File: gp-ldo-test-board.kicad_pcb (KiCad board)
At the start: 2 copper layers, 38.1 x 25.4 mm, 58 parts, among them J1 Conn_01x03, J2 Conn_01x02, J3 Conn_01x06, J4 Conn_01x02, J5 Conn_01x06, J6 Conn_01x02, J7 Conn_01x02, J8 Conn_01x02, J9 Conn_01x02, Q1 Q_PMOS_GSD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

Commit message: initial route draft
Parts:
- moved R3 9.96 mm to (51.6, 59.8), turned to 270 degrees
- moved R4 9.05 mm to (51.6, 63.3), turned to 270 degrees
- moved D3 5.50 mm to (79.9, 57.0)
- moved D5 5.50 mm to (79.9, 67.0)
- moved D7 5.50 mm to (79.9, 59.0)
- moved D9 5.50 mm to (79.9, 69.0)
- moved R10 5.50 mm to (77.0, 57.0)
- moved R12 5.50 mm to (77.0, 67.0)
- moved R14 5.50 mm to (77.0, 59.0)
- moved R16 5.50 mm to (77.0, 69.0)
- moved J6 5.08 mm to (86.3, 56.9)
- moved J7 5.08 mm to (86.3, 51.8)
- moved J8 5.08 mm to (86.3, 67.0)
- moved J9 5.08 mm to (86.3, 61.9)
- moved D10 4.50 mm to (79.9, 64.0)
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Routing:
- net /V_3.3_MGMT: track 0.00 -> 79.2 mm, vias 0 -> 1
- net +5V: track 0.00 -> 71.5 mm, vias 0 -> 2
- net GND: track 0.00 -> 45.1 mm, vias 0 -> 13
- net /SLG1_SCL: track 0.00 -> 32.8 mm, vias 0 -> 1
- net /CTRL_SDA: track 0.00 -> 27.0 mm, vias 0 -> 2
- net /V_Vccio1: track 0.00 -> 26.0 mm
- net /SLG1_SDA: track 0.00 -> 25.7 mm, vias 0 -> 1
- net /CTRL_SCL: track 0.00 -> 25.3 mm, vias 0 -> 2
- net /V_Vccio2: track 0.00 -> 24.8 mm
- net Net-(J5-Pad1): track 0.00 -> 24.7 mm, vias 0 -> 1
- net /V_3.3_MGMT_FAULT: track 0.00 -> 24.5 mm, vias 0 -> 2
- net /V_1.8_Vcore: track 0.00 -> 21.9 mm
- net Net-(J3-Pad5): track 0.00 -> 21.5 mm, vias 0 -> 1
- net Net-(Q1-Pad3): track 0.00 -> 17.1 mm, vias 0 -> 3
- net /V_Vccio1_FAULT: track 0.00 -> 14.4 mm, vias 0 -> 2
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- added copper zone on B.Cu, net GND
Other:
- net class power added: clearance 0.1524, trace_width 0.254, via_dia 0.762, via_drill 0.381

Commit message: route major cleanup
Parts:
- moved TP4 2.50 mm to (64.0, 51.6)
- moved D1 2.50 mm to (58.5, 72.9)
- moved D2 2.50 mm to (61.0, 72.9)
- moved R7 2.50 mm to (58.5, 70.0)
- moved R8 2.50 mm to (61.0, 70.0)
- moved TP3 0.30 mm to (64.0, 53.8)
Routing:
- net /AUX_LED_1: track 11.8 -> 5.86 mm
- net /AUX_LED_0: track 5.69 -> 9.05 mm
- net +5V: track 71.5 -> 68.5 mm
- net /V_1.8_Vcore_FAULT: track 11.3 -> 14.2 mm
- net /SLG1_SCL: track 32.8 -> 30.0 mm
- net Net-(Q1-Pad3): track 17.1 -> 14.5 mm
- net /CTRL_SDA: track 27.0 -> 25.4 mm, vias 2 -> 1
- net /CTRL_SCL: track 25.3 -> 23.9 mm, vias 2 -> 1
- net Net-(J3-Pad5): track 21.5 -> 22.5 mm
- net Net-(J3-Pad1): track 7.26 -> 8.26 mm, vias 1 -> 0
- net Net-(TP1-Pad1): track 4.57 -> 3.59 mm
- net GND: track 45.1 -> 44.3 mm
- net /SLG0_SDA: track 11.8 -> 12.5 mm
- net /V_Vccio1_FAULT: track 14.4 -> 13.7 mm

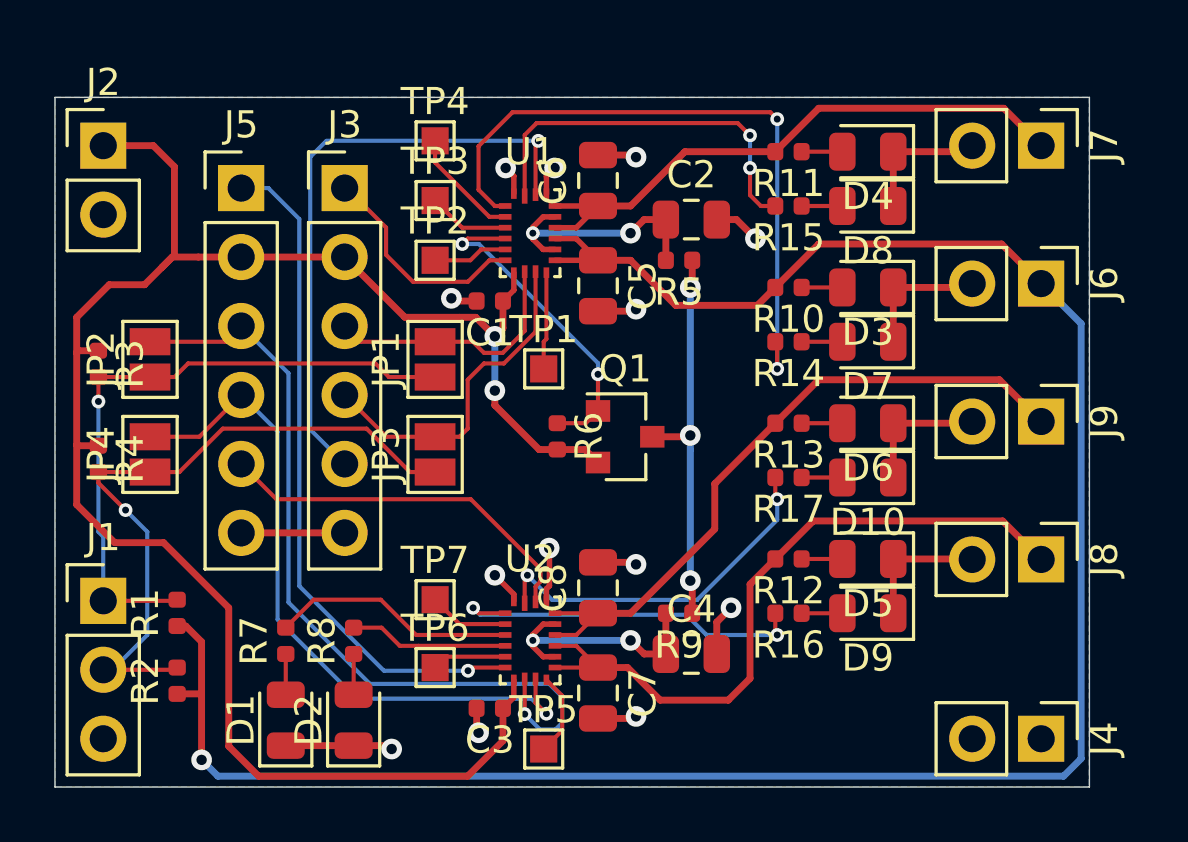
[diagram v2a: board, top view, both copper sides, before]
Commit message: silk cleanup
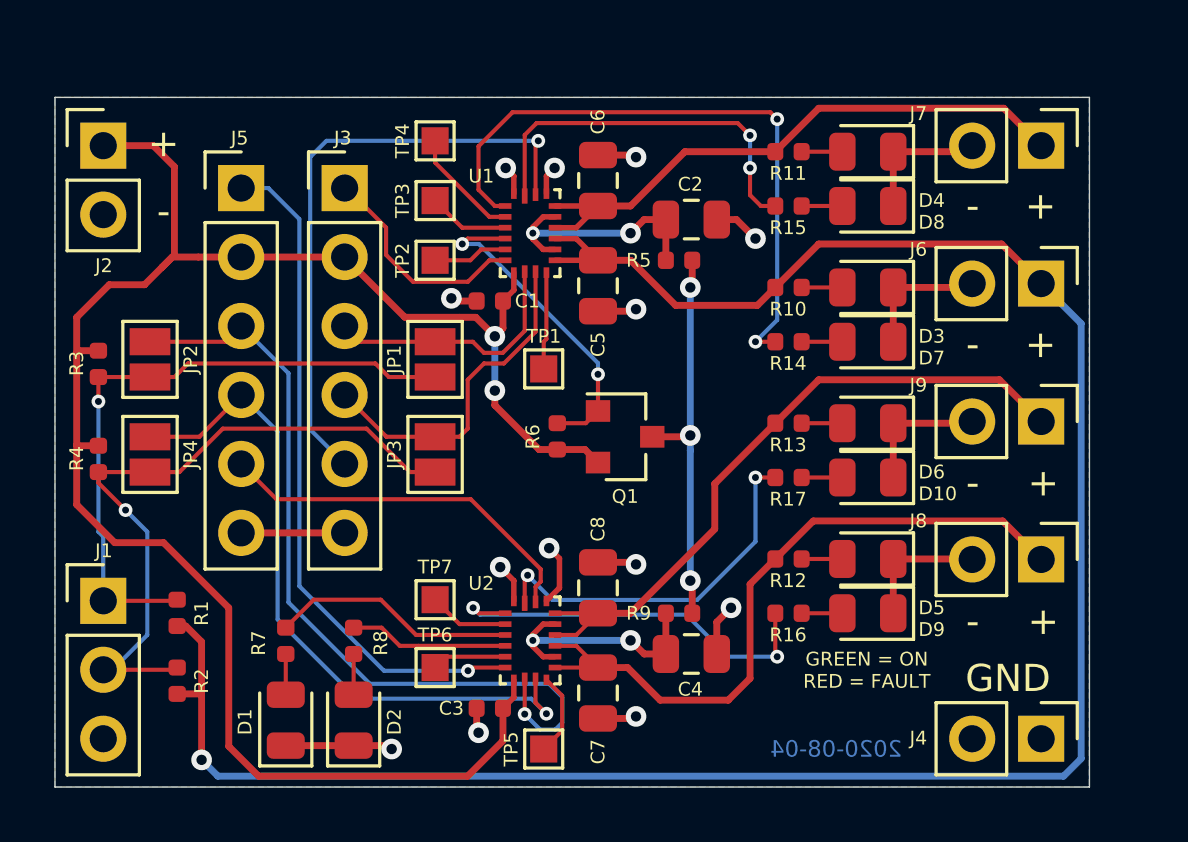
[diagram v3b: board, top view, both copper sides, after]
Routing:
- net /V_Vccio1_FAULT: track 13.7 -> 14.8 mm
- net /V_3.3_MGMT_FAULT: track 24.7 -> 23.7 mm
- net GND: track 44.3 -> 44.8 mm
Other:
- board text added: "+"
- board text added: "+1.5V-3.3V out "Vccio1""
- board text added: "+1.5V-3.3V out "Vccio2""
- board text added: "+1.8V out "Vcore""
- board text added: "+3.3V out "Vmgmt""
- board text added: "+5V"
- board text added: "+5V in"
- board text added: "-"
- board text added: "2020-08-04"
- board text added: "GND"
- board text added: "GREEN = ON RED = FAULT"
- board text added: "MODE P18"
- board text added: "SCL"
- board text added: "SCL P8"
- board text added: "SDA"
- board text added: "SDA P9"
- board text added: "SLG46582 GreenPAK LDO test board"
- board text added: "Vpp P6"
- board text added: "for U1"
- board text added: "for U2"
